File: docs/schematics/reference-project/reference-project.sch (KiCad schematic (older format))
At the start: 22 parts, among them J1 UART, Q1 MMBT3904, SW1 INPUT_0, SW2 INPUT_1, SW3 INPUT_2, SW4 INPUT_3, SW5 INPUT_4, SW6 INPUT_5, SW7 RESET, U1 74HC165D, U2 ATTINY85-20PU

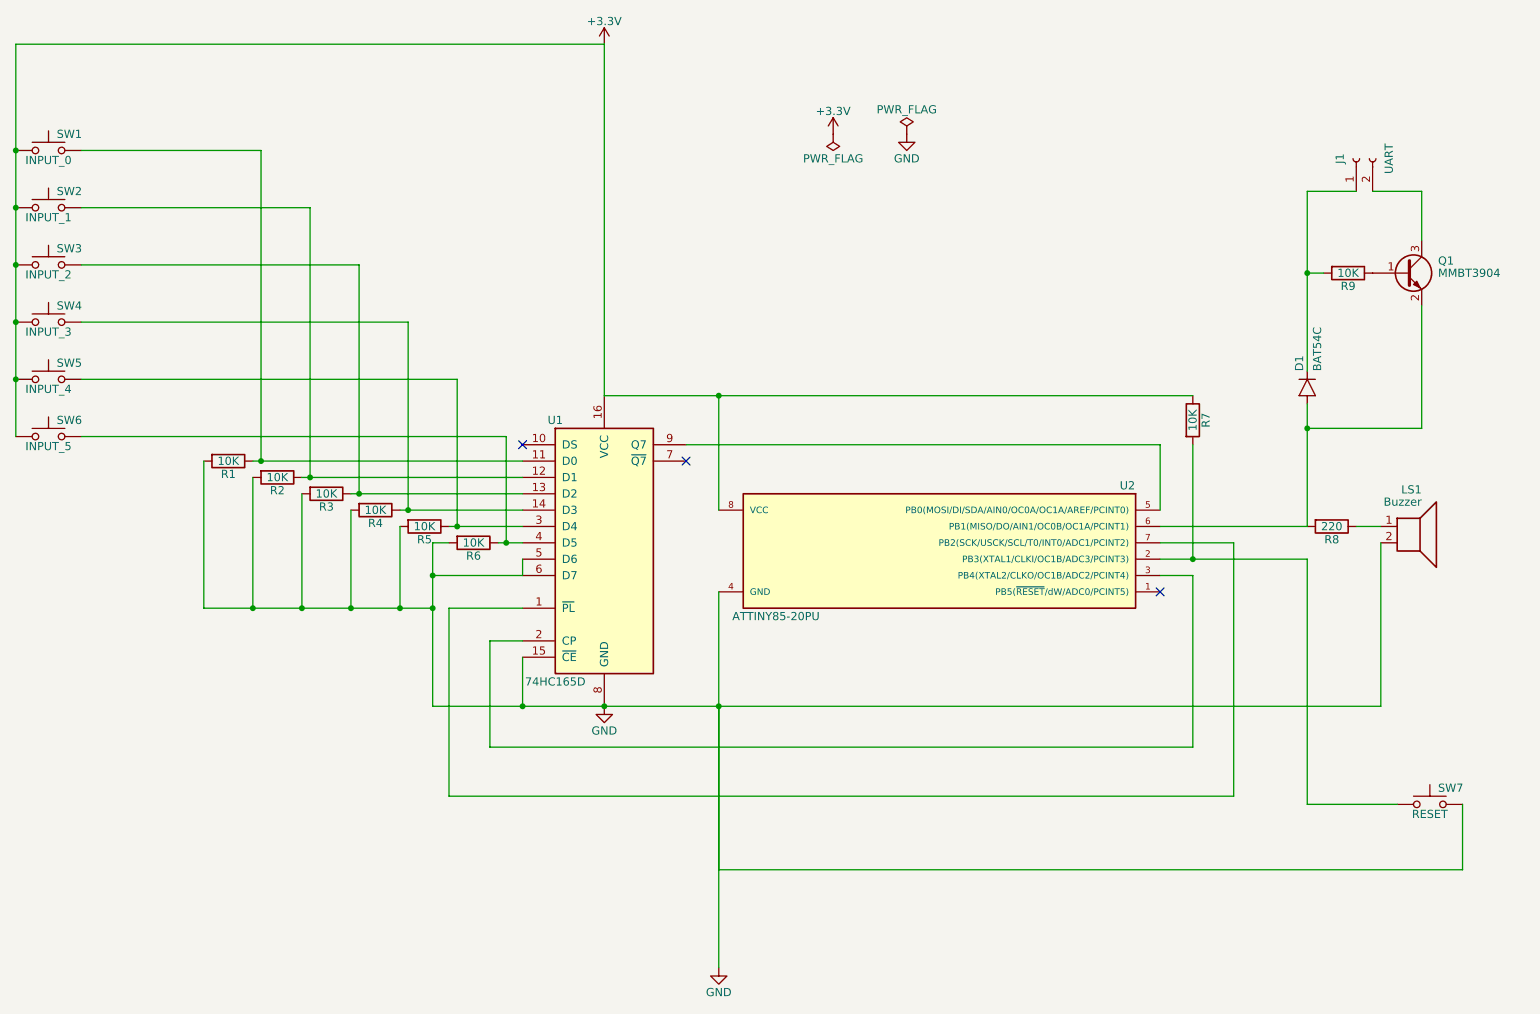
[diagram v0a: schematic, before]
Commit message: New version of schematics.
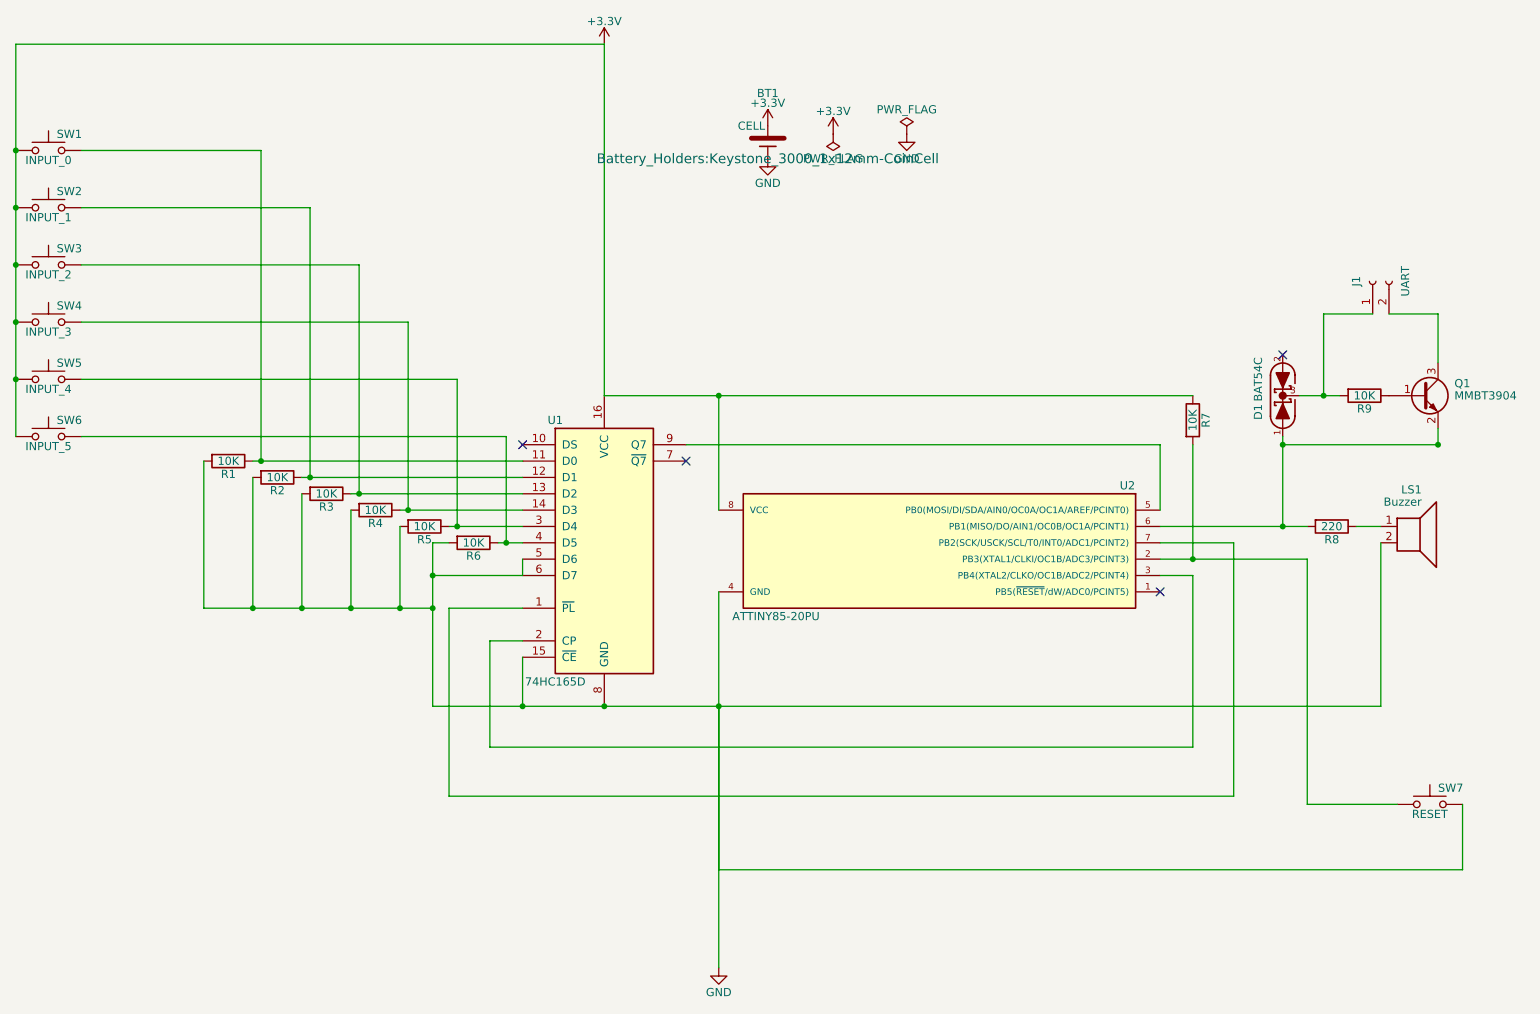
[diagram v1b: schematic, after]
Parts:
- removed D1: BAT54C, DIODE-1N4148, symbol DIODE1N4148
- added BT1: CELL, Battery_Holders:Keystone_3000_1x12mm-CoinCell, symbol CELL
- added D1: BAT54C, smd-semi:SOT-23, symbol BAT54C
- J1: footprint (none) -> footprints:Header_2_Pin
- LS1: footprint (none) -> Buzzers_Beepers:Buzzer_12x9.5RM7.6
- R1, R2, R3, R4, R5, R6, R7, R8, R9: footprint (none) -> Resistors_SMD:R_0805_HandSoldering
- SW1, SW2, SW3, SW4, SW5, SW6, SW7: footprint (none) -> Buttons_Switches_SMD:SW_SPST_TL3342
- U1: footprint (none) -> footprints:SOIC_16_0.154IN
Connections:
- net +3V3: now also BT1.1 (+)
- net GND: now also BT1.2 (-)
- net at Q1.2 (E), R8.2, U2.6 (PB1(MISO/DO/AIN1/OC0B/OC1A/PCINT1)): now also D1.1 (A1)
- net at J1.1 (Pin_1), R9.2: now also D1.3 (COM)
- no-connect marks 3 -> 4
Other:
- moved on the sheet: J1, Q1, R9

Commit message: Finished schematics.
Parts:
- BT1: footprint Battery_Holders:Keystone_3000_1x12mm-CoinCell -> Connectors:bornier2
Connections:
- net at U1.7 (~Q7): now also U2.5 (PB0(MOSI/DI/SDA/AIN0/OC0A/OC1A/AREF/PCINT0))
- net at U1.9 (Q7): no longer U2.5 (PB0(MOSI/DI/SDA/AIN0/OC0A/OC1A/AREF/PCINT0))
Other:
- moved on the sheet: R7
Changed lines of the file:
@@
 L R R7
 U 1 1 59E587BF
-P 8950 3350
-F 0 "R7" V 9030 3350 50  0000 C CNN
-F 1 "10K" V 8950 3350 50  0000 C CNN
-F 2 "Resistors_SMD:R_0805_HandSoldering" V 8880 3350 50  0001 C CNN
-F 3 "" H 8950 3350 50  0001 C CNN
-	1    8950 3350
+P 8850 3350
+F 0 "R7" V 8930 3350 50  0000 C CNN
+F 1 "10K" V 8850 3350 50  0000 C CNN
+F 2 "Resistors_SMD:R_0805_HandSoldering" V 8780 3350 50  0001 C CNN
+F 3 "" H 8850 3350 50  0001 C CNN
+	1    8850 3350
 	1    0    0    -1
 $EndComp
@@
 	1    0    0    -1
 $EndComp
-NoConn ~ 5850 3600
 NoConn ~ 8750 4400
 NoConn ~ 4850 3500
@@
 	0    -1   -1   0
 $EndComp
-Wire Wire Line
-	4300 5100 10100 5100
-Wire Wire Line
-	6050 4400 6050 6100
-Connection ~ 5350 5100
-Wire Wire Line
-	5850 3500 8750 3500
-Wire Wire Line
-	8750 3500 8750 3900
-Wire Wire Line
-	4850 4700 4650 4700
-Wire Wire Line
-	4650 4700 4650 5350
-Wire Wire Line
-	4650 5350 8950 5350
-Wire Wire Line
-	8950 5350 8950 4300
-Wire Wire Line
-	8950 4300 8750 4300
-Wire Wire Line
-	4300 4500 2900 4500
-Wire Wire Line
-	4400 5650 9200 5650
-Wire Wire Line
-	9200 5650 9200 4100
-Wire Wire Line
-	9200 4100 8750 4100
-Wire Wire Line
-	4400 4000 4850 4000
-Wire Wire Line
-	4100 3900 4850 3900
-Wire Wire Line
-	3800 3800 4850 3800
-Wire Wire Line
-	3500 3700 4850 3700
-Wire Wire Line
-	4100 4500 4100 4000
-Wire Wire Line
-	3800 3900 3800 4500
-Connection ~ 4100 4500
-Wire Wire Line
-	3500 3800 3500 4500
-Connection ~ 3800 4500
-Wire Wire Line
-	3200 3700 3200 4500
-Connection ~ 3500 4500
-Wire Wire Line
-	2900 4500 2900 3600
-Connection ~ 3200 4500
-Wire Wire Line
-	3200 3600 4850 3600
-Wire Wire Line
-	4700 4100 4850 4100
-Wire Wire Line
-	4750 4100 4750 3450
-Wire Wire Line
-	4750 3450 2150 3450
-Connection ~ 4750 4100
-Wire Wire Line
-	4450 4000 4450 3100
-Wire Wire Line
-	4450 3100 2150 3100
-Connection ~ 4450 4000
-Wire Wire Line
-	4150 3900 4150 2750
-Wire Wire Line
-	4150 2750 2150 2750
-Connection ~ 4150 3900
-Wire Wire Line
-	3850 3800 3850 2400
-Wire Wire Line
-	3850 2400 2150 2400
-Connection ~ 3850 3800
-Wire Wire Line
-	3550 3700 3550 2050
-Wire Wire Line
-	3550 2050 2150 2050
-Connection ~ 3550 3700
-Wire Wire Line
-	3250 3600 3250 1700
-Wire Wire Line
-	3250 1700 2150 1700
-Connection ~ 3250 3600
-Wire Wire Line
-	1750 1050 1750 3450
-Connection ~ 1750 2050
-Connection ~ 1750 2400
-Connection ~ 1750 2750
-Connection ~ 1750 3100
-Wire Wire Line
-	4400 4500 4400 5650
-Wire Wire Line
-	4850 4500 4400 4500
-Wire Wire Line
-	4300 4100 4400 4100
-Wire Wire Line
-	4300 4100 4300 5100
-Connection ~ 4300 4500
-Wire Wire Line
-	4850 4800 4850 5100
-Connection ~ 4850 5100
-Wire Wire Line
-	4850 4200 4850 4300
-Wire Wire Line
-	4850 4300 4300 4300
-Connection ~ 4300 4300
-Connection ~ 6050 5100
-Wire Wire Line
-	1750 1050 5350 1050
-Wire Wire Line
-	5350 1050 5350 3200
-Connection ~ 1750 1700
-Wire Wire Line
-	10450 3500 10450 3400
-Wire Wire Line
-	10450 3000 10450 2700
-Wire Wire Line
-	10100 5100 10100 4100
-Wire Wire Line
-	8750 4200 9650 4200
-Wire Wire Line
-	8950 3500 8950 4200
-Wire Wire Line
-	9950 4000 10100 4000
-Wire Wire Line
-	9650 4200 9650 5700
-Wire Wire Line
-	9650 5700 10200 5700
-Connection ~ 8950 4200
-Wire Wire Line
-	6050 6100 10600 6100
-Wire Wire Line
-	10600 6100 10600 5700
-Wire Wire Line
-	6050 5100 6050 6700
-Wire Wire Line
-	9750 2700 10050 2700
-Wire Wire Line
-	10450 2700 10150 2700
-Wire Wire Line
-	5350 3200 8950 3200
 $Comp
 L +3.3V #PWR02
@@
 	1    0    0    -1
 $EndComp
-Wire Wire Line
-	6050 3900 6050 3200
-Connection ~ 6050 3200
 $Comp
 L +3.3V #PWR03
@@
 	0    1    -1   0
 $EndComp
-Wire Wire Line
-	9500 3450 9500 4000
-Wire Wire Line
-	9600 3200 9850 3200
-Wire Wire Line
-	9750 2700 9750 3200
-Connection ~ 9750 3200
 NoConn ~ 9500 2950
-Wire Wire Line
-	10450 3500 9500 3500
-Connection ~ 9500 3500
-Connection ~ 10450 3500
-Wire Wire Line
-	8750 4000 9650 4000
-Connection ~ 9500 4000
 $Comp
 L PWR_FLAG #FLG05
@@
 F 0 "BT1" H 6350 1950 50  0000 C CNN
 F 1 "CELL" H 6250 1750 50  0000 C CNN
-F 2 "Battery_Holders:Keystone_3000_1x12mm-CoinCell" H 6350 1550 60  0000 C CNN
+F 2 "Connectors:bornier2" H 6350 1550 60  0000 C CNN
 F 3 "" H 6350 1550 60  0000 C CNN
 	1    6350 1650
@@
 	1    0    0    -1
 $EndComp
+NoConn ~ 5850 3500
+Wire Wire Line
+	4300 5100 10100 5100
+Wire Wire Line
+	6050 4400 6050 6100
+Wire Wire Line
+	4650 4500 4650 5350
+Wire Wire Line
+	4650 5350 8950 5350
+Wire Wire Line
+	4300 4500 2900 4500
+Wire Wire Line
+	8950 4100 8750 4100
+Wire Wire Line
+	4400 4000 4850 4000
+Wire Wire Line
+	4100 3900 4850 3900
+Wire Wire Line
+	3800 3800 4850 3800
+Wire Wire Line
+	3500 3700 4850 3700
+Wire Wire Line
+	4100 4500 4100 4000
+Wire Wire Line
+	3800 3900 3800 4500
+Connection ~ 4100 4500
+Wire Wire Line
+	3500 3800 3500 4500
+Connection ~ 3800 4500
+Wire Wire Line
+	3200 3700 3200 4500
+Connection ~ 3500 4500
+Wire Wire Line
+	2900 4500 2900 3600
+Connection ~ 3200 4500
+Wire Wire Line
+	3200 3600 4850 3600
+Wire Wire Line
+	4700 4100 4850 4100
+Wire Wire Line
+	4750 4100 4750 3450
+Wire Wire Line
+	4750 3450 2150 3450
+Connection ~ 4750 4100
+Wire Wire Line
+	4450 4000 4450 3100
+Wire Wire Line
+	4450 3100 2150 3100
+Connection ~ 4450 4000
+Wire Wire Line
+	4150 3900 4150 2750
+Wire Wire Line
+	4150 2750 2150 2750
+Connection ~ 4150 3900
+Wire Wire Line
+	3850 3800 3850 2400
+Wire Wire Line
+	3850 2400 2150 2400
+Connection ~ 3850 3800
+Wire Wire Line
+	3550 3700 3550 2050
+Wire Wire Line
+	3550 2050 2150 2050
+Connection ~ 3550 3700
+Wire Wire Line
+	3250 3600 3250 1700
+Wire Wire Line
+	3250 1700 2150 1700
+Connection ~ 3250 3600
+Wire Wire Line
+	1750 1050 1750 3450
+Connection ~ 1750 2050
+Connection ~ 1750 2400
+Connection ~ 1750 2750
+Connection ~ 1750 3100
+Wire Wire Line
+	4400 4700 4400 5650
+Wire Wire Line
+	4300 4100 4400 4100
+Wire Wire Line
+	4300 4100 4300 5100
+Connection ~ 4300 4500
+Wire Wire Line
+	4850 5100 4850 4800
+Connection ~ 4850 5100
+Wire Wire Line
+	4850 4200 4850 4300
+Wire Wire Line
+	4850 4300 4300 4300
+Connection ~ 4300 4300
+Wire Wire Line
+	1750 1050 5350 1050
+Wire Wire Line
+	5350 1050 5350 3200
+Connection ~ 1750 1700
+Wire Wire Line
+	10450 3500 10450 3400
+Wire Wire Line
+	10450 3000 10450 2700
+Wire Wire Line
+	10100 5100 10100 4100
+Wire Wire Line
+	8750 4200 9650 4200
+Wire Wire Line
+	9950 4000 10100 4000
+Wire Wire Line
+	9650 4200 9650 5700
+Wire Wire Line
+	9650 5700 10200 5700
+Wire Wire Line
+	6050 6100 10600 6100
+Wire Wire Line
+	10600 6100 10600 5700
+Wire Wire Line
+	6050 5100 6050 6700
+Wire Wire Line
+	9750 2700 10050 2700
+Wire Wire Line
+	10450 2700 10150 2700
+Wire Wire Line
+	5350 3200 8850 3200
+Wire Wire Line
+	6050 3200 6050 3900
+Wire Wire Line
+	9500 3450 9500 4000
+Wire Wire Line
+	9600 3200 9850 3200
+Wire Wire Line
+	9750 2700 9750 3200
+Connection ~ 9750 3200
+Wire Wire Line
+	10450 3500 9500 3500
+Connection ~ 9500 3500
+Wire Wire Line
+	8750 4000 9650 4000
+Connection ~ 9500 4000
+Wire Wire Line
+	5850 3600 8750 3600
+Wire Wire Line
+	8750 3600 8750 3900
+Wire Wire Line
+	8850 4300 8750 4300
+Wire Wire Line
+	8850 4300 8850 5650
+Wire Wire Line
+	8850 5650 4400 5650
+Wire Wire Line
+	8950 5350 8950 4100
+Connection ~ 6050 3200
+Wire Wire Line
+	8850 3500 8850 4200
+Connection ~ 8850 4200
+Connection ~ 5350 5100
+Connection ~ 6050 5100
+Wire Wire Line
+	4650 4500 4850 4500
+Wire Wire Line
+	4400 4700 4850 4700
 $EndSCHEMATC

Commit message: Updated to v2.
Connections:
- net at U1.2 (CP): now also U2.5 (PB0(MOSI/DI/SDA/AIN0/OC0A/OC1A/AREF/PCINT0)); no longer U2.3 (PB4(XTAL2/CLKO/OC1B/ADC2/PCINT4))
- net at U1.7 (~Q7): now also U2.3 (PB4(XTAL2/CLKO/OC1B/ADC2/PCINT4)); no longer U2.5 (PB0(MOSI/DI/SDA/AIN0/OC0A/OC1A/AREF/PCINT0))
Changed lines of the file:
@@
 Connection ~ 1750 3100
-Wire Wire Line
-	4400 4700 4400 5650
 Wire Wire Line
 	4300 4100 4400 4100
@@
 Connection ~ 9500 4000
 Wire Wire Line
-	5850 3600 8750 3600
-Wire Wire Line
-	8750 3600 8750 3900
-Wire Wire Line
-	8850 4300 8750 4300
-Wire Wire Line
-	8850 4300 8850 5650
-Wire Wire Line
-	8850 5650 4400 5650
-Wire Wire Line
 	8950 5350 8950 4100
 Connection ~ 6050 3200
@@
 	4650 4500 4850 4500
 Wire Wire Line
+	5850 3600 9050 3600
+Wire Wire Line
 	4400 4700 4850 4700
+Wire Wire Line
+	4400 4700 4400 5650
+Wire Wire Line
+	4400 5650 9150 5650
+Wire Wire Line
+	8750 4300 9050 4300
+Wire Wire Line
+	9050 4300 9050 3600
+Wire Wire Line
+	8750 3900 9150 3900
+Wire Wire Line
+	9150 3900 9150 5650
 $EndSCHEMATC

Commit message: Updated to v3.
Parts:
- removed D1: BAT54C, smd-semi:SOT-23, symbol BAT54C
- removed J1: UART, footprints:Header_2_Pin, symbol Conn_01x02_Female
- removed Q1: MMBT3904, TO_SOT_Packages_SMD:SOT-23, symbol MMBT3904
- removed R1, R2, R3, R4, R5, R9: 10K, Resistors_SMD:R_0805_HandSoldering, symbol R
- removed SW1: INPUT_0, Buttons_Switches_SMD:SW_SPST_TL3342, symbol SW_Push
- removed SW2: INPUT_1, Buttons_Switches_SMD:SW_SPST_TL3342, symbol SW_Push
- removed SW3: INPUT_2, Buttons_Switches_SMD:SW_SPST_TL3342, symbol SW_Push
- removed SW4: INPUT_3, Buttons_Switches_SMD:SW_SPST_TL3342, symbol SW_Push
- removed SW5: INPUT_4, Buttons_Switches_SMD:SW_SPST_TL3342, symbol SW_Push
- removed U1: 74HC165D, footprints:SOIC_16_0.154IN, symbol 74LS165
- renumbered R7 to R1, R6 to R2, R8 to R3, SW7 to SW1, SW6 to SW2, U2 to U1
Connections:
- net +3V3: now also SW2.2; no longer SW2.1
- net GND: now also SW1.1; no longer SW1.2
- net at R1.2, U1.2 (PB3(XTAL1/CLKI/OC1B/ADC3/PCINT3)): now also SW1.2; no longer SW1.1
- net at R2.1: now also SW2.1, U1.3 (PB4(XTAL2/CLKO/OC1B/ADC2/PCINT4)); no longer SW2.2
- no-connect marks 4 -> 3
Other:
- moved on the sheet: R1, R2, SW1, SW2
